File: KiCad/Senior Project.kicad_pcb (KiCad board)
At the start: 4 copper layers, 34 x 46.8 mm, 68 parts, among them J1 USB_C_Receptacle_USB2.0_16P, J2 Screw_Terminal_01x02, J3 Screw_Terminal_01x06, Q2 IRLML0030, Q3 IRLML0030, Q4 IRLML0030, SW1 SW_Push, SW2 SW_Push, U1 ESP32-S3FH4R2, U2 TPS62162DSG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

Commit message: PCB update
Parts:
- U6: moved to F.Cu
- moved U6 57.9 mm to (148.3, 82.2)
- moved U3 27.6 mm to (113.0, 64.6)
- moved AE2 18.7 mm to (103.0, 50.9)
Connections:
- J1 pad A4: +BATT -> Net-(D1-K)
- J1 pad A9: +BATT -> Net-(D1-K)
- J1 pad B4: +BATT -> Net-(D1-K)
- J1 pad B9: +BATT -> Net-(D1-K)
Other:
- board size 34 x 46.8 mm -> 50 x 67 mm

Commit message: Fixes
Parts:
- C23, J2, J3, Q2, Q3, Q4: moved to F.Cu
- moved C23 53.0 mm to (150.1, 62.8)
- moved Q4 42.5 mm to (135.9, 96.3)
- moved C6 42.2 mm to (43.0, 81.7)
- moved R5 42.2 mm to (43.6, 80.3)
- moved U1 42.2 mm to (47.3, 75.8)
- moved Q3 39.9 mm to (132.8, 91.9)
- moved Q2 36.5 mm to (129.6, 96.9)
- moved J3 35.1 mm to (134.1, 101.8), turned to -90 degrees
- moved C19 33.5 mm to (61.6, 115.3)
- moved L4 33.5 mm to (62.2, 110.5)
- moved R2 33.5 mm to (56.2, 116.1)
- moved R3 33.5 mm to (56.2, 114.9)
- moved U2 33.5 mm to (59.0, 114.5)
- moved C18 33.5 mm to (59.6, 117.7)
- moved R6 33.5 mm to (61.8, 113.1)
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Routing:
- net GND: track 181.1 -> 0.00 mm, vias 15 -> 0
- net +3V3: track 175.8 -> 0.00 mm, vias 6 -> 0
- net /SCL: track 56.3 -> 0.00 mm, vias 4 -> 0
- net /SDA: track 55.9 -> 0.00 mm, vias 4 -> 0
- net /Sense 1: track 49.0 -> 0.00 mm, vias 2 -> 0
- net /Interrupt: track 48.6 -> 0.00 mm, vias 2 -> 0
- net /RADIO_RST: track 41.6 -> 0.00 mm, vias 2 -> 0
- net /Pyro GPIO 2: track 30.2 -> 0.00 mm, vias 2 -> 0
- net /Sense 2: track 29.7 -> 0.00 mm, vias 2 -> 0
- net Net-(JP2-B): track 25.1 -> 0.00 mm, vias 2 -> 0
- net /Sense 3: track 21.7 -> 0.00 mm, vias 2 -> 0
- net Net-(U1-VDD_SPI): track 21.6 -> 0.00 mm, vias 2 -> 0
- net Net-(JP1-B): track 21.1 -> 0.00 mm, vias 2 -> 0
- net /Pyro GPIO 1: track 20.4 -> 0.00 mm, vias 2 -> 0
- net /FSPICS0: track 19.5 -> 0.00 mm, vias 2 -> 0
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- removed copper zone on B.Cu, net GND
- removed copper zone on F.Cu, net GND
- removed copper zone on In2.Cu, net GND

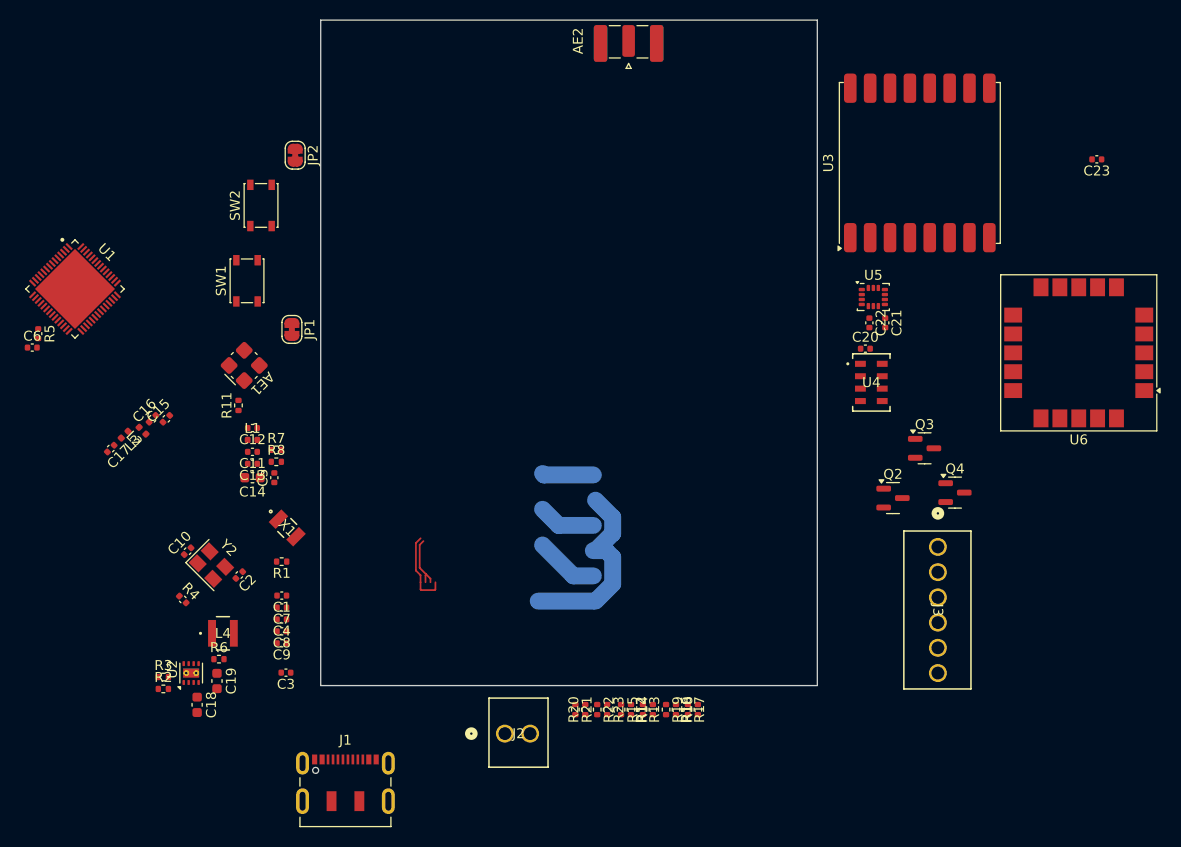
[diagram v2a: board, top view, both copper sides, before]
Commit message: removed traces
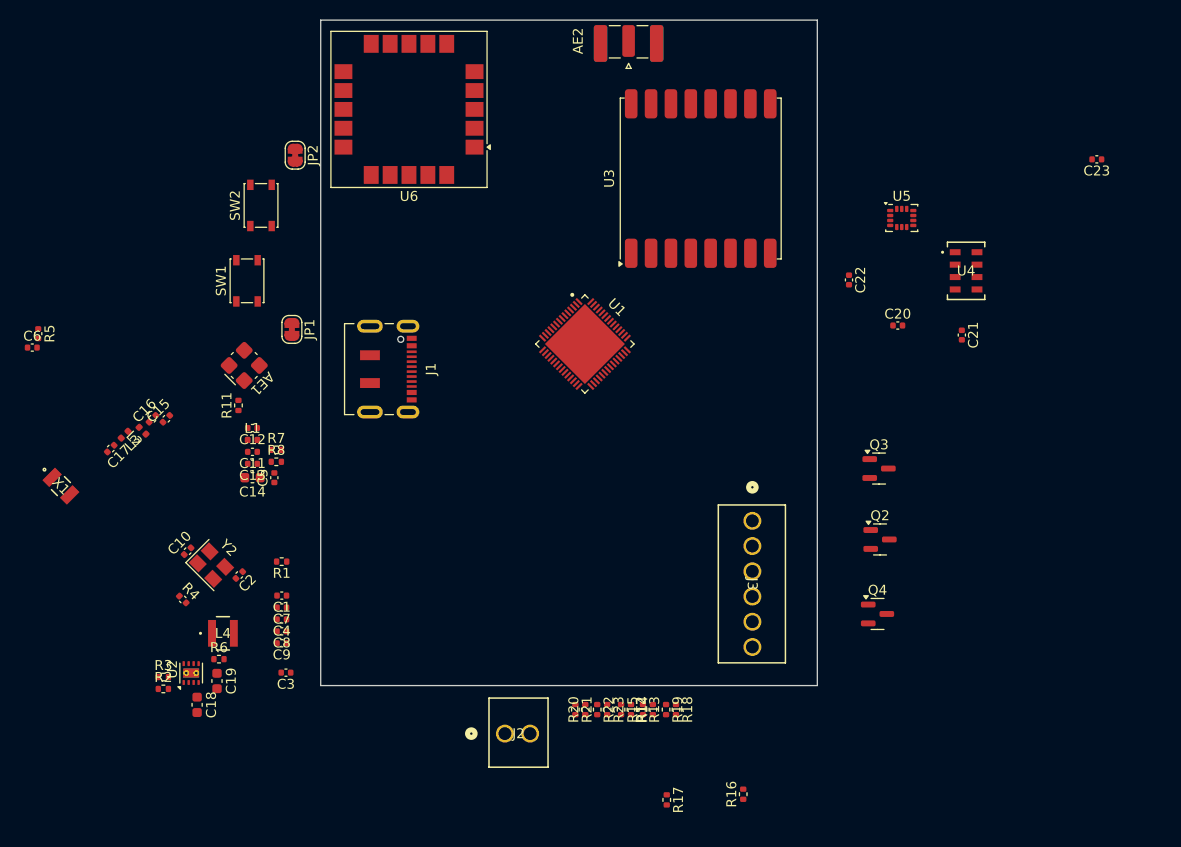
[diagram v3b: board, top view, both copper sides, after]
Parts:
- moved U6 71.7 mm to (80.9, 57.7)
- moved U1 51.6 mm to (98.6, 81.4)
- moved J1 42.5 mm to (78.1, 83.9), turned to -90 degrees
- moved X1 23.2 mm to (45.8, 95.7)
- moved U3 22.1 mm to (110.3, 64.7)
- moved J3 18.9 mm to (115.5, 99.2)
- moved U4 14.7 mm to (137.0, 74.0)
- moved Q4 14.5 mm to (128.1, 108.5)
- moved R16 9.67 mm to (114.5, 126.7)
- moved R17 9.34 mm to (106.8, 127.3)
- moved U5 8.46 mm to (130.5, 68.7)
- moved C21 7.81 mm to (136.6, 80.5)
- moved Q3 5.02 mm to (128.2, 93.9)
- moved C22 4.78 mm to (125.2, 74.9)
- moved Q2 4.37 mm to (128.3, 101.0)
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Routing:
- net +BATT: track 19.4 -> 0.00 mm
- net /USB_D-: track 7.81 -> 0.00 mm
- net /Pyro Channel1/Pyro Pin: track 6.40 -> 0.00 mm
- net /Pyro Channel2/Pyro Pin: track 5.78 -> 0.00 mm
- net /USB_D+: track 5.57 -> 0.00 mm
- net /Pyro Channel3/Pyro Pin: track 5.17 -> 0.00 mm
